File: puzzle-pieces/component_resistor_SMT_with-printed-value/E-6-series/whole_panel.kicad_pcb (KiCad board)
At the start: 2 copper layers, 210 x 210 mm, 175 parts, among them J1 Conn_01x02_Pin, J10 Conn_01x02_Pin, J11 Conn_01x02_Pin, J12 Conn_01x02_Pin, J13 Conn_01x02_Pin, J14 Conn_01x02_Pin, J15 Conn_01x02_Pin, J16 Conn_01x02_Pin, J17 Conn_01x02_Pin, J18 Conn_01x02_Pin, J19 Conn_01x02_Pin, J2 Conn_01x02_Pin, J20 Conn_01x02_Pin, J21 Conn_01x02_Pin, J22 Conn_01x02_Pin, J23 Conn_01x02_Pin, J24 Conn_01x02_Pin, J25 Conn_01x02_Pin, J26 Conn_01x02_Pin, J27 Conn_01x02_Pin, J28 Conn_01x02_Pin, J29 Conn_01x02_Pin, J3 Conn_01x02_Pin, J30 Conn_01x02_Pin, J31 Conn_01x02_Pin, J32 Conn_01x02_Pin, J33 Conn_01x02_Pin, J34 Conn_01x02_Pin, J35 Conn_01x02_Pin, J36 Conn_01x02_Pin, J37 Conn_01x02_Pin, J38 Conn_01x02_Pin, J39 Conn_01x02_Pin, J4 Conn_01x02_Pin, J40 Conn_01x02_Pin, J41 Conn_01x02_Pin, J42 Conn_01x02_Pin, J43 Conn_01x02_Pin, J44 Conn_01x02_Pin, J45 Conn_01x02_Pin, J46 Conn_01x02_Pin, J47 Conn_01x02_Pin, J48 Conn_01x02_Pin, J49 Conn_01x02_Pin, J5 Conn_01x02_Pin, J50 Conn_01x02_Pin, J6 Conn_01x02_Pin, J7 Conn_01x02_Pin, J8 Conn_01x02_Pin, J9 Conn_01x02_Pin

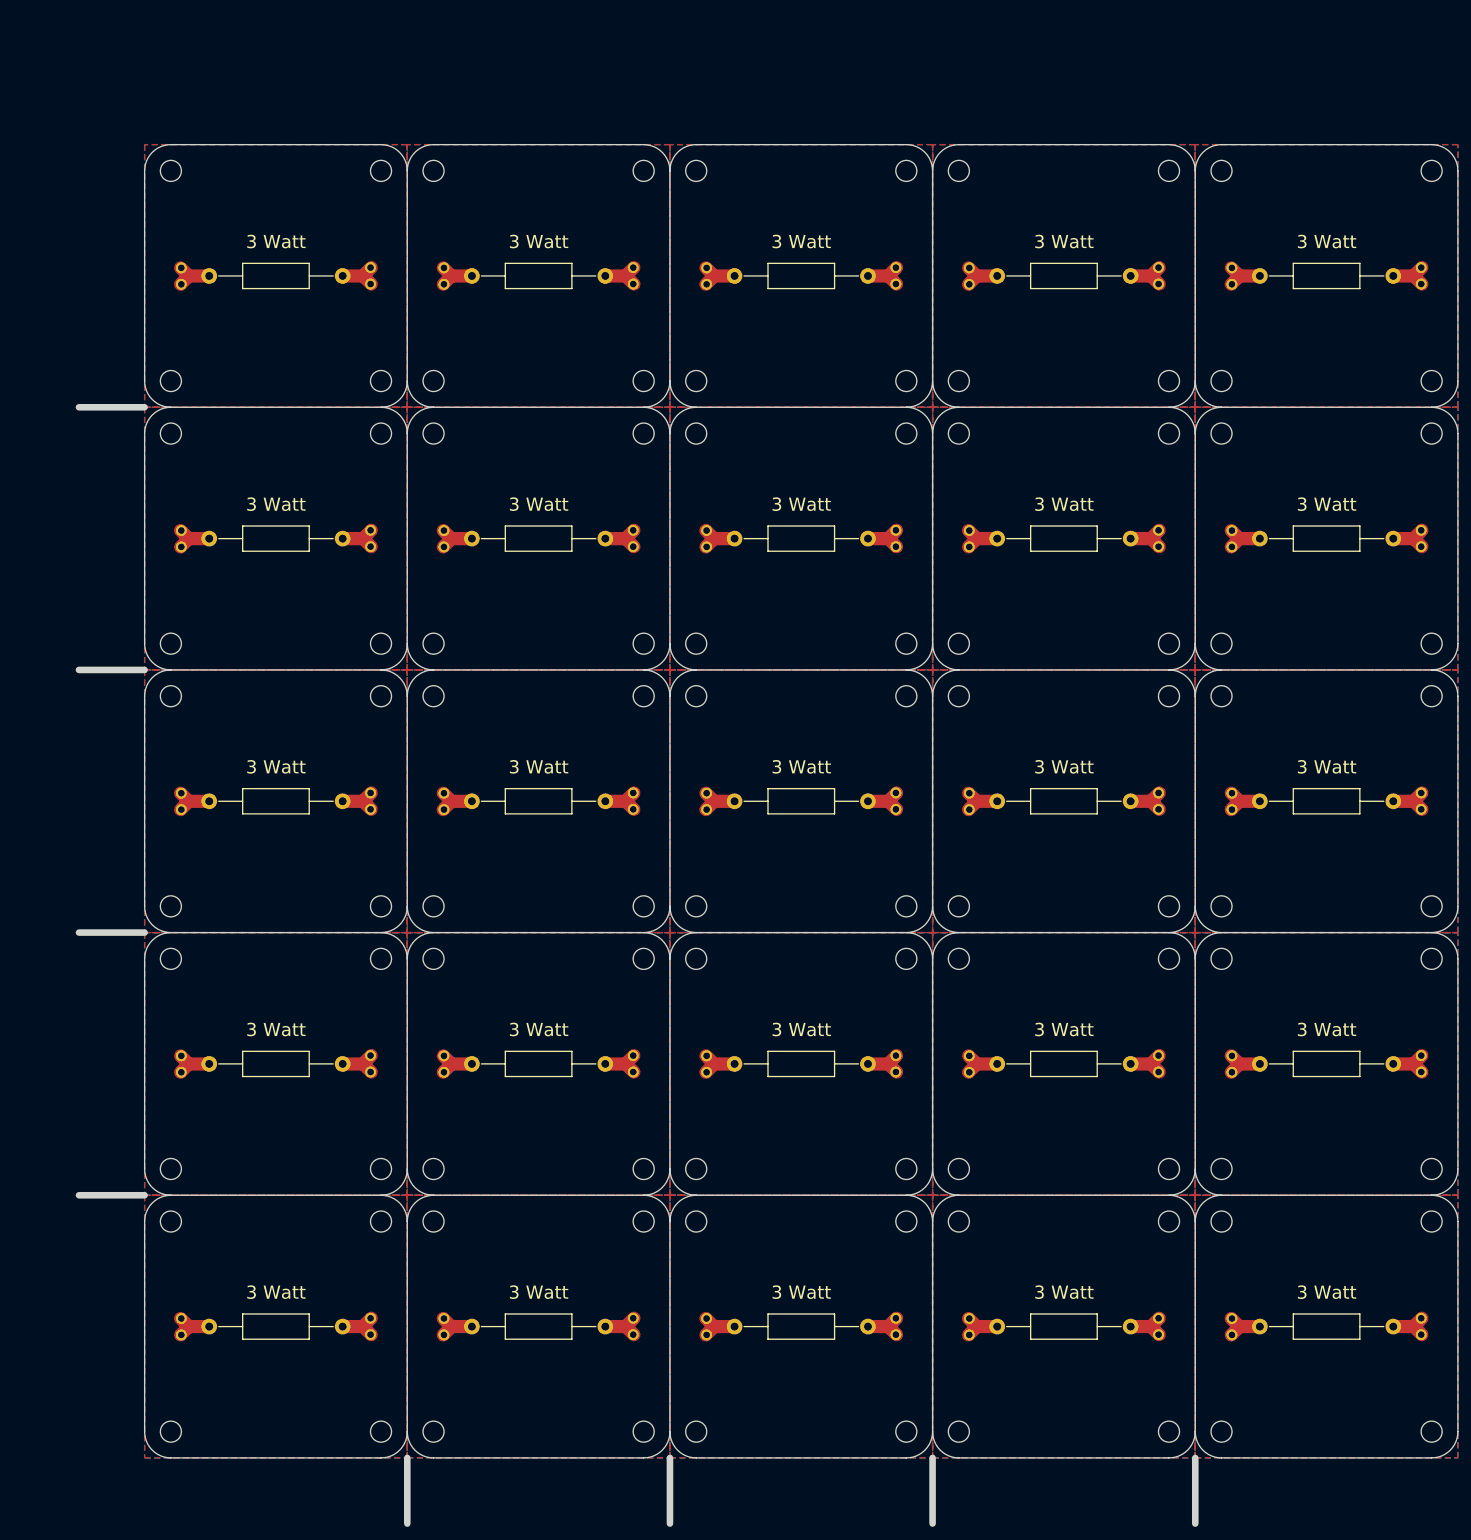
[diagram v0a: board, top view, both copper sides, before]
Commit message: Update PCB layout and mounting hole positions
Revised mounting hole locations and references, updated connector and resistor placements, and removed/re-added production zip file. These changes improve board layout consistency and mechanical fit.
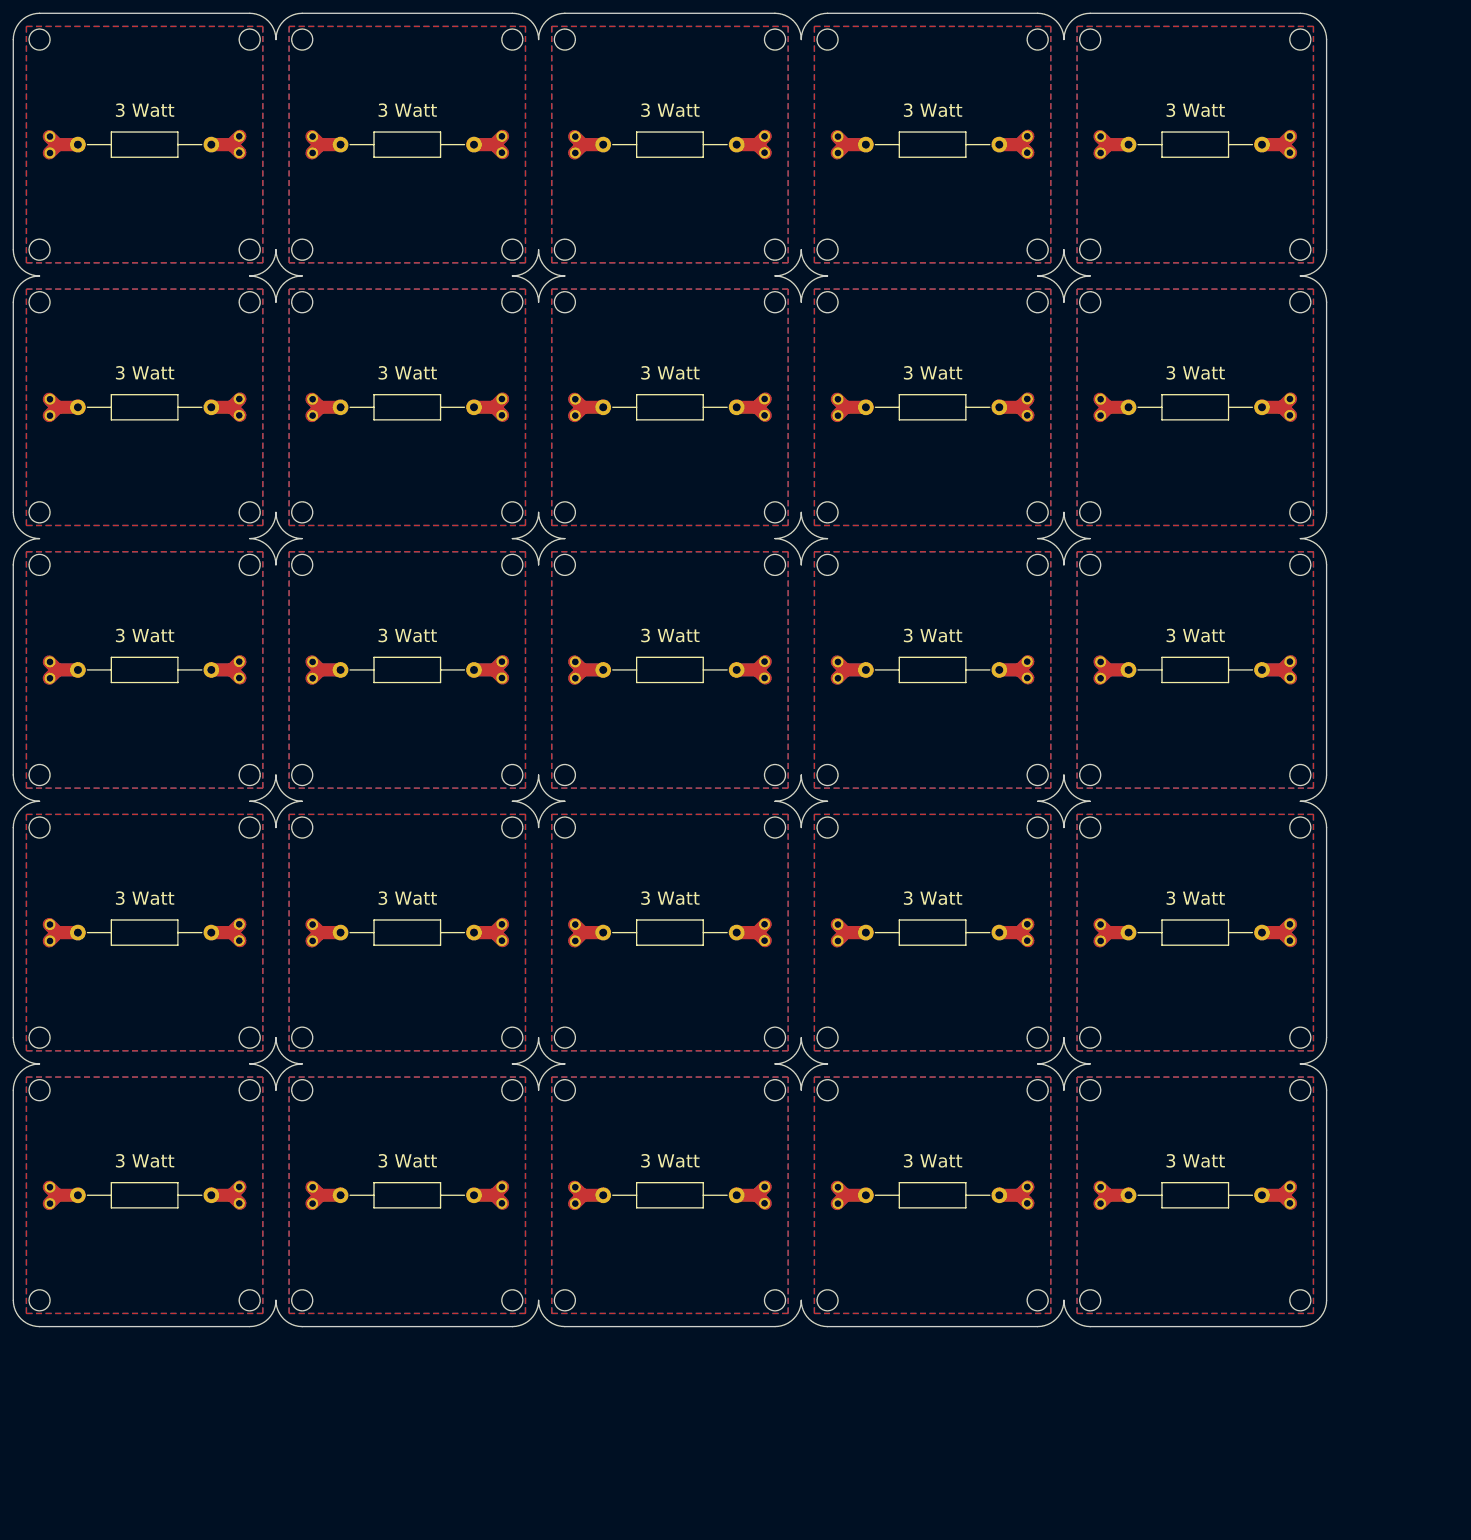
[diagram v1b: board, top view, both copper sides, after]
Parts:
- removed H1, H10, H100, H11, H12, H13, H14, H15, H16, H17, H18, H19, H2, H20, H21, H22, H23, H24, H25, H26, H27, H28, H29, H3, H30, H31, H32, H33, H34, H35, H36, H37, H38, H39, H4, H40, H41, H42, H43, H44, H45, H46, H47, H48, H49, H50, H51, H52, H53, H54, H55, H56, H57, H58, H59, H6, H60, H61, H62, H63, H64, H65, H66, H67, H68, H69, H7, H70, H71, H72, H73, H74, H75, H76, H77, H78, H79, H8, H80, H81, H82, H83, H84, H85, H86, H87, H88, H89, H9, H90, H91, H92, H93, H94, H95, H96, H97, H98, H99: MH M3, MountingHole:MountingHole_3.2mm_M3
- added H5: MH M3, MountingHole:MountingHole_3.2mm_M3, F.Cu at (4.00, 84.0)
- added H5: MH M3, MountingHole:MountingHole_3.2mm_M3, F.Cu at (76.0, 124.0)
- added H5: MH M3, MountingHole:MountingHole_3.2mm_M3, F.Cu at (44.0, 36.0)
- added H5: MH M3, MountingHole:MountingHole_3.2mm_M3, F.Cu at (36.0, 164.0)
- added H5: MH M3, MountingHole:MountingHole_3.2mm_M3, F.Cu at (84.0, 164.0)
- added H5: MH M3, MountingHole:MountingHole_3.2mm_M3, F.Cu at (116.0, 116.0)
- added H5: MH M3, MountingHole:MountingHole_3.2mm_M3, F.Cu at (76.0, 164.0)
- added H5: MH M3, MountingHole:MountingHole_3.2mm_M3, F.Cu at (36.0, 76.0)
- added H5: MH M3, MountingHole:MountingHole_3.2mm_M3, F.Cu at (116.0, 4.00)
- added H5: MH M3, MountingHole:MountingHole_3.2mm_M3, F.Cu at (164.0, 116.0)
- added H5: MH M3, MountingHole:MountingHole_3.2mm_M3, F.Cu at (124.0, 76.0)
- added H5: MH M3, MountingHole:MountingHole_3.2mm_M3, F.Cu at (116.0, 196.0)
- added H5: MH M3, MountingHole:MountingHole_3.2mm_M3, F.Cu at (44.0, 164.0)
- added H5: MH M3, MountingHole:MountingHole_3.2mm_M3, F.Cu at (124.0, 156.0)
- added H5: MH M3, MountingHole:MountingHole_3.2mm_M3, F.Cu at (116.0, 164.0)
- added H5: MH M3, MountingHole:MountingHole_3.2mm_M3, F.Cu at (116.0, 44.0)
- added H5: MH M3, MountingHole:MountingHole_3.2mm_M3, F.Cu at (76.0, 4.00)
- added H5: MH M3, MountingHole:MountingHole_3.2mm_M3, F.Cu at (196.0, 124.0)
- added H5: MH M3, MountingHole:MountingHole_3.2mm_M3, F.Cu at (156.0, 36.0)
- added H5: MH M3, MountingHole:MountingHole_3.2mm_M3, F.Cu at (84.0, 196.0)
- added H5: MH M3, MountingHole:MountingHole_3.2mm_M3, F.Cu at (36.0, 156.0)
- added H5: MH M3, MountingHole:MountingHole_3.2mm_M3, F.Cu at (124.0, 116.0)
- added H5: MH M3, MountingHole:MountingHole_3.2mm_M3, F.Cu at (44.0, 76.0)
- added H5: MH M3, MountingHole:MountingHole_3.2mm_M3, F.Cu at (84.0, 156.0)
- added H5: MH M3, MountingHole:MountingHole_3.2mm_M3, F.Cu at (116.0, 156.0)
- added H5: MH M3, MountingHole:MountingHole_3.2mm_M3, F.Cu at (84.0, 124.0)
- added H5: MH M3, MountingHole:MountingHole_3.2mm_M3, F.Cu at (196.0, 44.0)
- added H5: MH M3, MountingHole:MountingHole_3.2mm_M3, F.Cu at (36.0, 84.0)
- added H5: MH M3, MountingHole:MountingHole_3.2mm_M3, F.Cu at (4.00, 164.0)
- added H5: MH M3, MountingHole:MountingHole_3.2mm_M3, F.Cu at (164.0, 36.0)
- added H5: MH M3, MountingHole:MountingHole_3.2mm_M3, F.Cu at (4.00, 116.0)
- added H5: MH M3, MountingHole:MountingHole_3.2mm_M3, F.Cu at (164.0, 124.0)
- added H5: MH M3, MountingHole:MountingHole_3.2mm_M3, F.Cu at (196.0, 116.0)
- added H5: MH M3, MountingHole:MountingHole_3.2mm_M3, F.Cu at (76.0, 156.0)
- added H5: MH M3, MountingHole:MountingHole_3.2mm_M3, F.Cu at (164.0, 164.0)
- added H5: MH M3, MountingHole:MountingHole_3.2mm_M3, F.Cu at (164.0, 156.0)
- added H5: MH M3, MountingHole:MountingHole_3.2mm_M3, F.Cu at (4.00, 36.0)
- added H5: MH M3, MountingHole:MountingHole_3.2mm_M3, F.Cu at (76.0, 116.0)
- added H5: MH M3, MountingHole:MountingHole_3.2mm_M3, F.Cu at (124.0, 84.0)
- added H5: MH M3, MountingHole:MountingHole_3.2mm_M3, F.Cu at (76.0, 36.0)
- added H5: MH M3, MountingHole:MountingHole_3.2mm_M3, F.Cu at (124.0, 44.0)
- added H5: MH M3, MountingHole:MountingHole_3.2mm_M3, F.Cu at (36.0, 36.0)
- added H5: MH M3, MountingHole:MountingHole_3.2mm_M3, F.Cu at (164.0, 44.0)
- added H5: MH M3, MountingHole:MountingHole_3.2mm_M3, F.Cu at (124.0, 124.0)
- added H5: MH M3, MountingHole:MountingHole_3.2mm_M3, F.Cu at (44.0, 4.00)
- added H5: MH M3, MountingHole:MountingHole_3.2mm_M3, F.Cu at (124.0, 196.0)
- added H5: MH M3, MountingHole:MountingHole_3.2mm_M3, F.Cu at (4.00, 196.0)
- added H5: MH M3, MountingHole:MountingHole_3.2mm_M3, F.Cu at (156.0, 156.0)
- added H5: MH M3, MountingHole:MountingHole_3.2mm_M3, F.Cu at (124.0, 4.00)
- added H5: MH M3, MountingHole:MountingHole_3.2mm_M3, F.Cu at (164.0, 76.0)
- added H5: MH M3, MountingHole:MountingHole_3.2mm_M3, F.Cu at (124.0, 164.0)
- added H5: MH M3, MountingHole:MountingHole_3.2mm_M3, F.Cu at (84.0, 84.0)
- added H5: MH M3, MountingHole:MountingHole_3.2mm_M3, F.Cu at (36.0, 124.0)
- added H5: MH M3, MountingHole:MountingHole_3.2mm_M3, F.Cu at (4.00, 124.0)
- added H5: MH M3, MountingHole:MountingHole_3.2mm_M3, F.Cu at (116.0, 76.0)
- added H5: MH M3, MountingHole:MountingHole_3.2mm_M3, F.Cu at (164.0, 84.0)
- added H5: MH M3, MountingHole:MountingHole_3.2mm_M3, F.Cu at (76.0, 44.0)
- added H5: MH M3, MountingHole:MountingHole_3.2mm_M3, F.Cu at (116.0, 84.0)
- added H5: MH M3, MountingHole:MountingHole_3.2mm_M3, F.Cu at (156.0, 116.0)
- added H5: MH M3, MountingHole:MountingHole_3.2mm_M3, F.Cu at (4.00, 44.0)
- added H5: MH M3, MountingHole:MountingHole_3.2mm_M3, F.Cu at (76.0, 84.0)
- added H5: MH M3, MountingHole:MountingHole_3.2mm_M3, F.Cu at (156.0, 76.0)
- added H5: MH M3, MountingHole:MountingHole_3.2mm_M3, F.Cu at (44.0, 116.0)
- added H5: MH M3, MountingHole:MountingHole_3.2mm_M3, F.Cu at (196.0, 4.00)
- added H5: MH M3, MountingHole:MountingHole_3.2mm_M3, F.Cu at (4.00, 156.0)
- added H5: MH M3, MountingHole:MountingHole_3.2mm_M3, F.Cu at (156.0, 164.0)
- added H5: MH M3, MountingHole:MountingHole_3.2mm_M3, F.Cu at (4.00, 76.0)
- added H5: MH M3, MountingHole:MountingHole_3.2mm_M3, F.Cu at (116.0, 124.0)
- added H5: MH M3, MountingHole:MountingHole_3.2mm_M3, F.Cu at (196.0, 84.0)
- added H5: MH M3, MountingHole:MountingHole_3.2mm_M3, F.Cu at (84.0, 116.0)
- added H5: MH M3, MountingHole:MountingHole_3.2mm_M3, F.Cu at (196.0, 196.0)
- added H5: MH M3, MountingHole:MountingHole_3.2mm_M3, F.Cu at (156.0, 196.0)
- added H5: MH M3, MountingHole:MountingHole_3.2mm_M3, F.Cu at (164.0, 4.00)
- added H5: MH M3, MountingHole:MountingHole_3.2mm_M3, F.Cu at (196.0, 36.0)
- added H5: MH M3, MountingHole:MountingHole_3.2mm_M3, F.Cu at (4.00, 4.00)
- added H5: MH M3, MountingHole:MountingHole_3.2mm_M3, F.Cu at (196.0, 164.0)
- added H5: MH M3, MountingHole:MountingHole_3.2mm_M3, F.Cu at (44.0, 44.0)
- added H5: MH M3, MountingHole:MountingHole_3.2mm_M3, F.Cu at (76.0, 76.0)
- added H5: MH M3, MountingHole:MountingHole_3.2mm_M3, F.Cu at (44.0, 196.0)
- added H5: MH M3, MountingHole:MountingHole_3.2mm_M3, F.Cu at (84.0, 76.0)
- added H5: MH M3, MountingHole:MountingHole_3.2mm_M3, F.Cu at (164.0, 196.0)
- added H5: MH M3, MountingHole:MountingHole_3.2mm_M3, F.Cu at (44.0, 84.0)
- added H5: MH M3, MountingHole:MountingHole_3.2mm_M3, F.Cu at (44.0, 124.0)
- added H5: MH M3, MountingHole:MountingHole_3.2mm_M3, F.Cu at (196.0, 76.0)
- added H5: MH M3, MountingHole:MountingHole_3.2mm_M3, F.Cu at (156.0, 84.0)
- added H5: MH M3, MountingHole:MountingHole_3.2mm_M3, F.Cu at (156.0, 44.0)
- added H5: MH M3, MountingHole:MountingHole_3.2mm_M3, F.Cu at (84.0, 44.0)
- added H5: MH M3, MountingHole:MountingHole_3.2mm_M3, F.Cu at (36.0, 196.0)
- added H5: MH M3, MountingHole:MountingHole_3.2mm_M3, F.Cu at (196.0, 156.0)
- added H5: MH M3, MountingHole:MountingHole_3.2mm_M3, F.Cu at (84.0, 36.0)
- added H5: MH M3, MountingHole:MountingHole_3.2mm_M3, F.Cu at (156.0, 4.00)
- added H5: MH M3, MountingHole:MountingHole_3.2mm_M3, F.Cu at (44.0, 156.0)
- added H5: MH M3, MountingHole:MountingHole_3.2mm_M3, F.Cu at (84.0, 4.00)
- added H5: MH M3, MountingHole:MountingHole_3.2mm_M3, F.Cu at (36.0, 116.0)
- added H5: MH M3, MountingHole:MountingHole_3.2mm_M3, F.Cu at (116.0, 36.0)
- added H5: MH M3, MountingHole:MountingHole_3.2mm_M3, F.Cu at (124.0, 36.0)
- added H5: MH M3, MountingHole:MountingHole_3.2mm_M3, F.Cu at (156.0, 124.0)
- added H5: MH M3, MountingHole:MountingHole_3.2mm_M3, F.Cu at (76.0, 196.0)
- added H5: MH M3, MountingHole:MountingHole_3.2mm_M3, F.Cu at (36.0, 44.0)
- moved J10 28.3 mm to (125.5, 20.0)
- moved J20 28.3 mm to (125.5, 60.0)
- moved J30 28.3 mm to (125.5, 100.0)
- moved J40 28.3 mm to (125.5, 140.0)
- moved J50 28.3 mm to (125.5, 180.0)
- moved H5 28.3 mm to (36.0, 4.00)
- moved J1 28.3 mm to (194.5, 180.0)
- moved J11 28.3 mm to (194.5, 20.0)
- moved J12 28.3 mm to (165.5, 20.0)
- moved J13 28.3 mm to (34.5, 60.0)
- moved J14 28.3 mm to (5.49, 60.0)
- moved J15 28.3 mm to (74.5, 60.0)
- moved J16 28.3 mm to (45.5, 60.0)
- moved J18 28.3 mm to (85.5, 60.0)
- moved J19 28.3 mm to (154.5, 60.0)
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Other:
- board size 210 x 210 mm -> 200 x 200 mm
- board text added: "2.2 kΩ"
